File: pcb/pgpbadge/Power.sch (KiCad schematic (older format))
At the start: 1 part

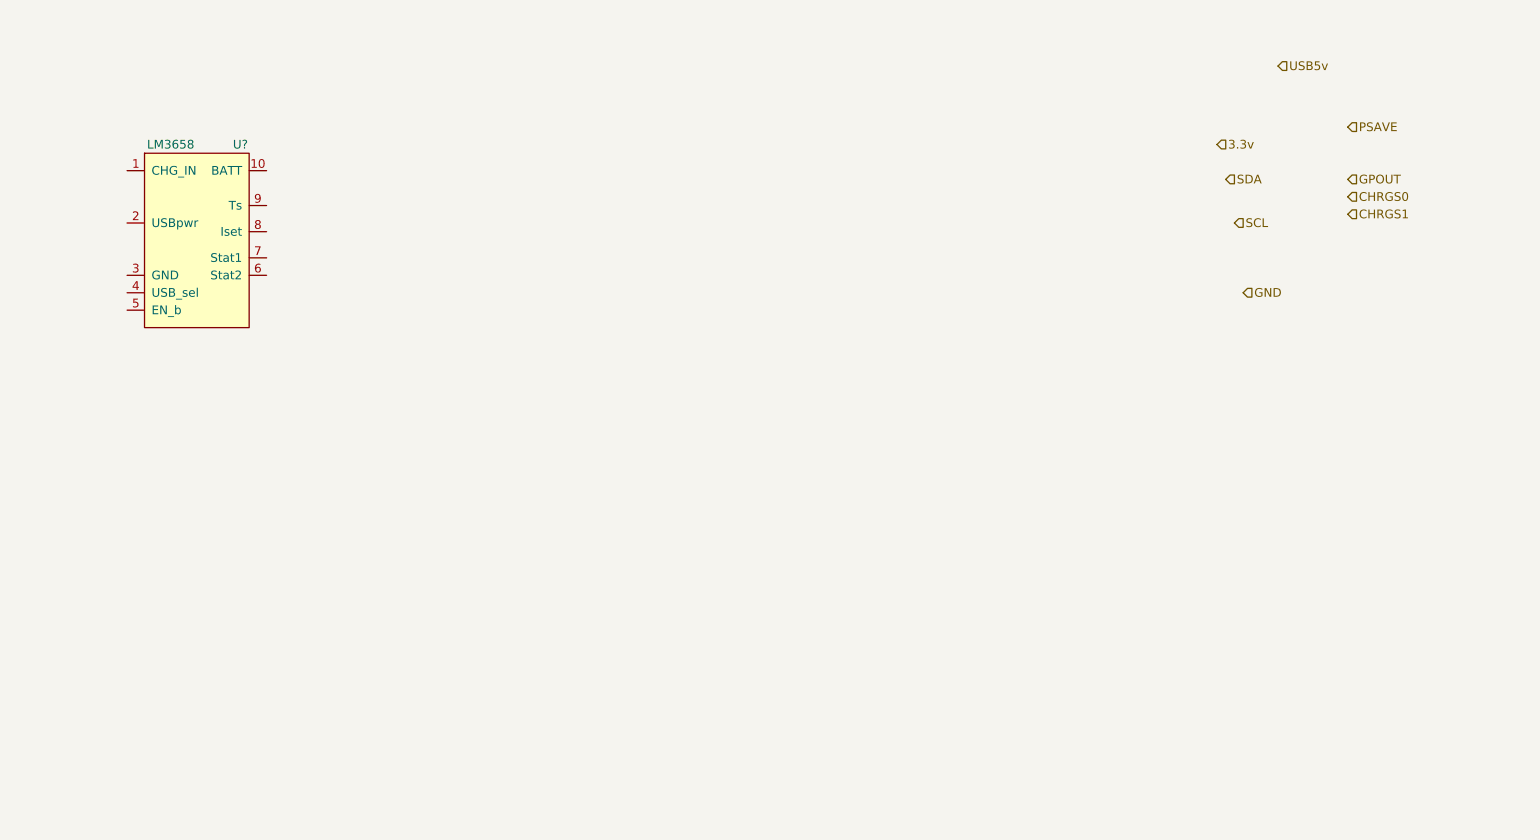
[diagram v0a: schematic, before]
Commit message: Board layout and routing done, need to fix DRC's, add more ground stitching, clean up silscreen, and review
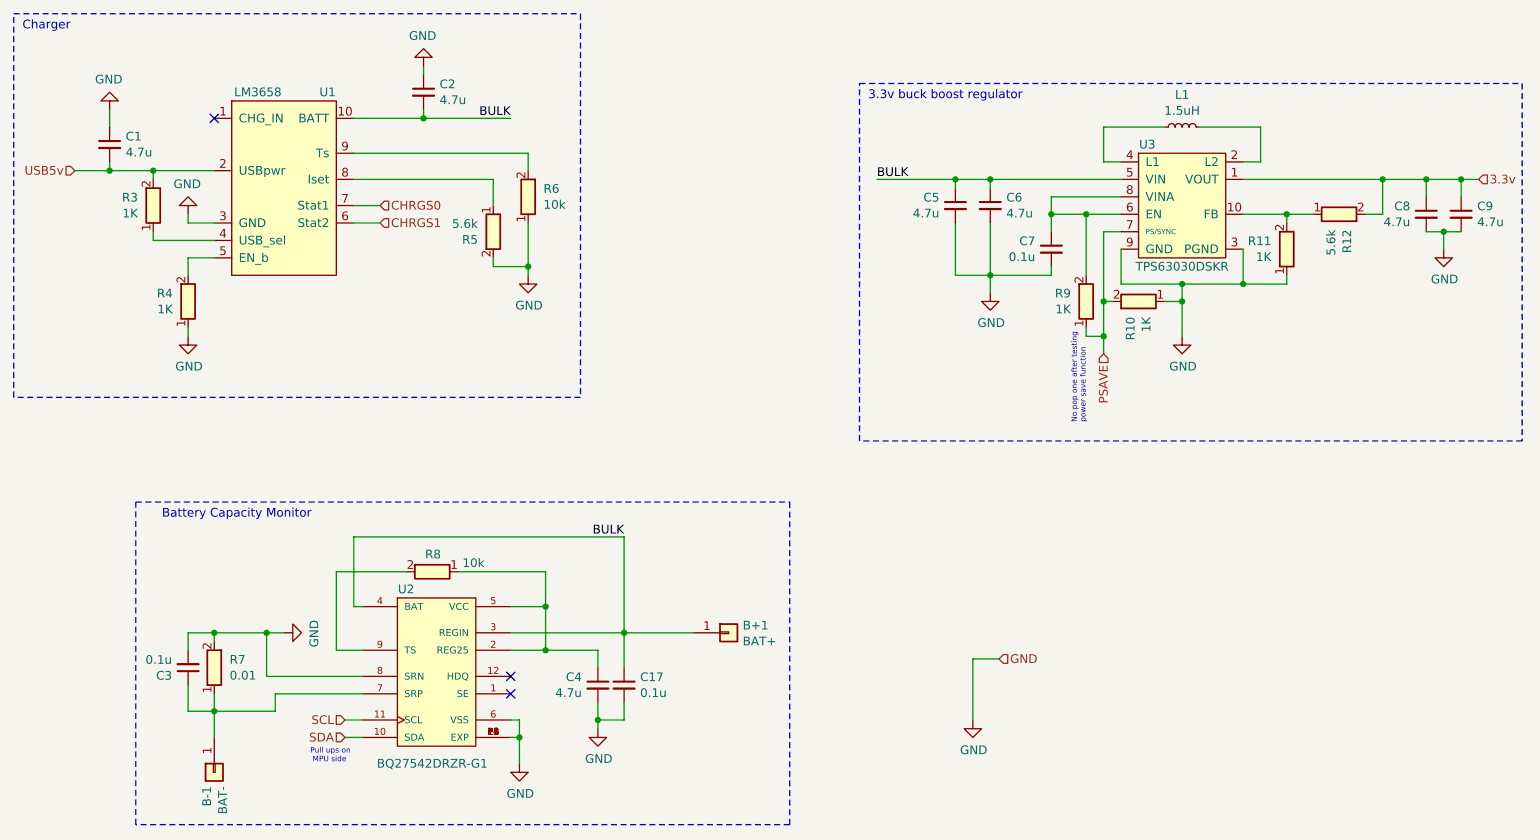
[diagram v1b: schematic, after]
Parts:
- added B+1: BAT+, pgpbadge:solder_pad, symbol Connector_Generic:Conn_01x01
- added B-1: BAT-, pgpbadge:solder_pad, symbol Connector_Generic:Conn_01x01
- added C1, C2, C4, C5, C6, C8, C9: 4.7u, Capacitor_SMD:C_0805_2012Metric, symbol Device:C_Small
- added C17, C3, C7: 0.1u, Capacitor_SMD:C_0402_1005Metric, symbol Device:C_Small
- added L1: 1.5uH, Inductor_SMD:L_1008_2520Metric, symbol Device:L_Small
- added R10, R11, R3, R4, R9: 1K, Resistor_SMD:R_0402_1005Metric, symbol pgpbadge:R
- added R12, R5: 5.6k, Resistor_SMD:R_0402_1005Metric, symbol pgpbadge:R
- added R6, R8: 10k, Resistor_SMD:R_0402_1005Metric, symbol pgpbadge:R
- added R7: 0.01, Resistor_SMD:R_1206_3216Metric, symbol pgpbadge:R
- added U2: BQ27542DRZR-G1, pgpbadge:SON40P250X400X100-13N, symbol pgpbadge:BQ27542DRZR-G1
- added U3: TPS63030DSKR, pgpbadge:10-WFDFN_EP_2.5_2.5, symbol pgpbadge:TPS63030DSKR
- gave numbers to parts that had none: 1
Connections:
- net 3.3v: now also C8.1, C9.1, R12.2, U3.1 (VOUT)
- net CHRGS0: now also U1.7 (Stat1)
- net CHRGS1: now also U1.6 (Stat2)
- net GND: now also U1.3 (GND), C1.1, C17.2, C2.1, C3.2, C4.2, C5.2, C6.2, C7.2, C8.2, C9.2, R10.1, R11.1, R4.1, R5.2, R6.1, R7.2, U2.13 (EXP), U2.14 (EXP), U2.15 (EXP), U2.6 (VSS), U2.8 (SRN), U2.P1 (EXP), U2.P2 (EXP), U2.P3 (EXP), U2.P4 (EXP), U2.P5 (EXP), U2.P6 (EXP), U3.3 (PGND), U3.9 (GND)
- net PSAVE: now also R10.2, R9.1, U3.7 (PS/SYNC)
- net SCL: now also U2.11 (SCL)
- net SDA: now also U2.10 (SDA)
- net USB5v: now also U1.2 (USBpwr), C1.2, R3.2
- net BULK: now reaches U1.10 (BATT)
- net BULK: now also B+1.1 (Pin_1), C17.1, C2.2, C5.1, C6.1, U2.3 (REGIN), U2.4 (BAT), U3.5 (VIN)
- net at U1.4 (USB_sel): now also R3.1
- net at U1.5 (EN_b): now also R4.2
- net at U1.8 (Iset): now also R5.1
- net at U1.9 (Ts): now also R6.2
- new net: L1.1, U3.4 (L1)
- new net: L1.2, U3.2 (L2)
- new net: R11.2, R12.1, U3.10 (FB)
- new net: C7.1, R9.2, U3.6 (EN), U3.8 (VINA)
- new net: B-1.1 (Pin_1), C3.1, R7.1, U2.7 (SRP)
- new net: C4.1, R8.1, U2.2 (REG25), U2.5 (VCC)
- new net: R8.2, U2.9 (TS)
- no-connect marks 0 -> 3
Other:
- note added: "3.3v buck boost regulator"
- note added: "Battery Capacity Monitor"
- note added: "Charger"
- note added: "No pop one after testing \npower save function"
- note added: "Pull ups on\n MPU side"
- moved on the sheet: U1
